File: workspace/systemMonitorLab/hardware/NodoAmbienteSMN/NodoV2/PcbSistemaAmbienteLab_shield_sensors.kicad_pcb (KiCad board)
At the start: 2 copper layers, 4 parts, among them J4 Molex_Sensor_BMP280, J5 Molex_Sensor_DHT22, U3 DHT22, U4 Bmp280Module

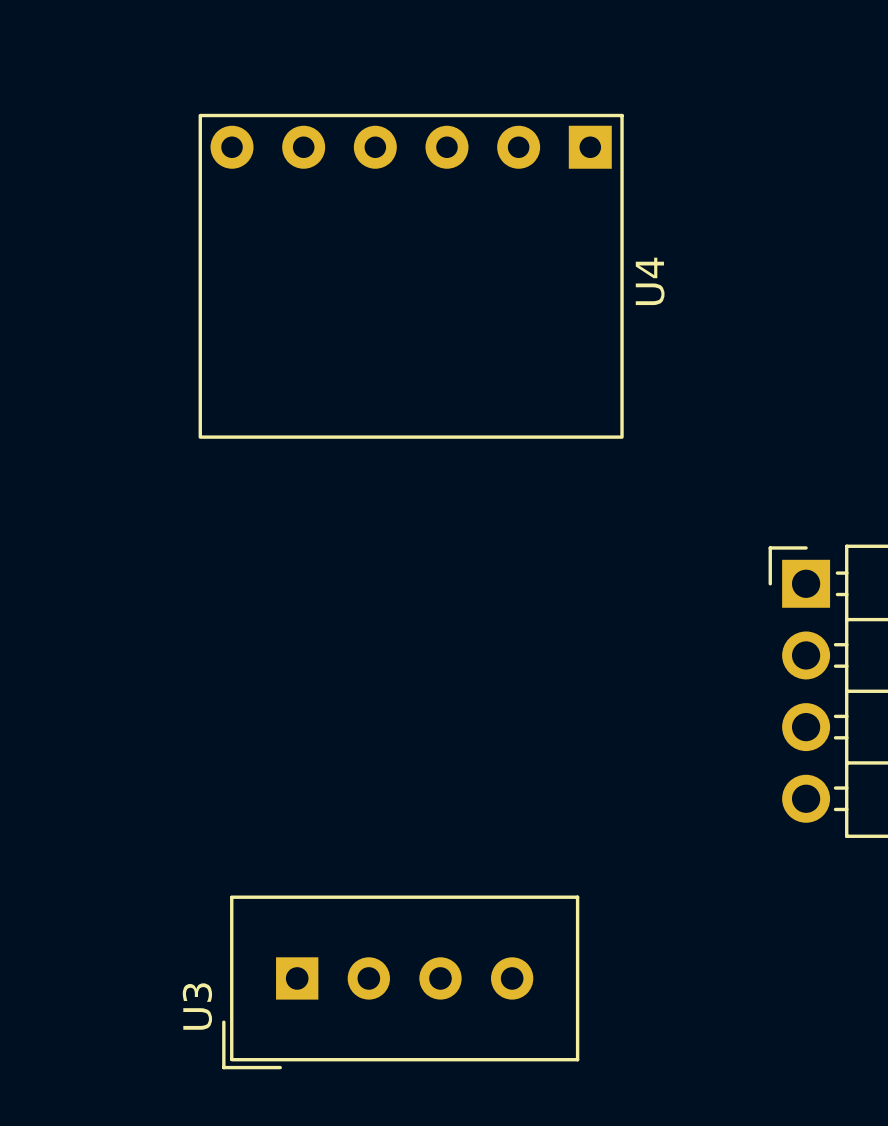
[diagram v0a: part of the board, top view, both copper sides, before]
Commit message: Se termino de generar el diseño de la placa shield_main_board.
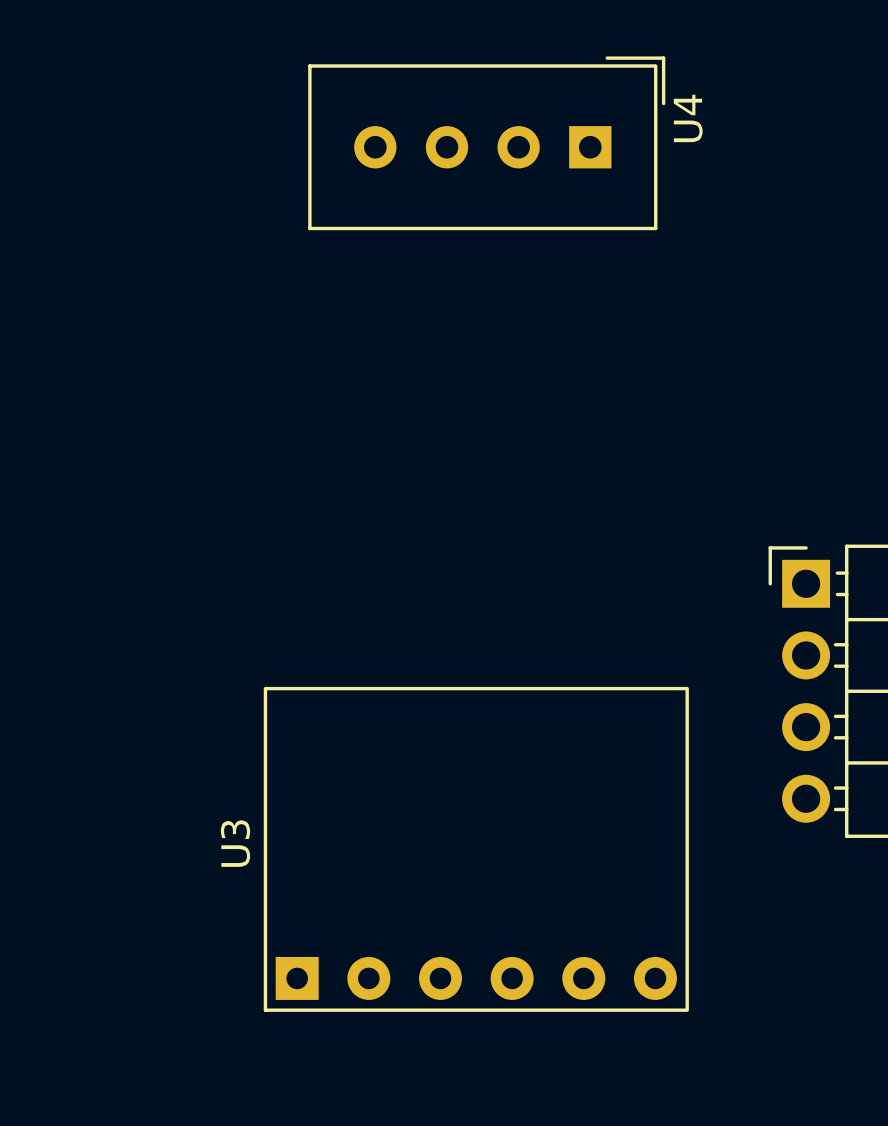
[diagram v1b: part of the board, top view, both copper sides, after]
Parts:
- U3: value DHT22 -> Bmp280Module; footprint Sensor:Aosong_DHT11_5.5x12.0_P2.54mm -> Sensors_commercial:BMP280_Module
- U4: value Bmp280Module -> DHT22; footprint Modulos:BMP280_Module -> Sensor:Aosong_DHT11_5.5x12.0_P2.54mm
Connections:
- U3 pad 2: Net-(J5-Pad2) -> GND
- U3 pad 3: unconnected-(U3-Pad3) -> Net-(J7-Pin_3)
- U3 pad 4: GND -> Net-(J7-Pin_4)
- U4 pad 1: 3V3 -> GND
- U4 pad 2: GND -> Net-(J9-Pin_2)
- U4 pad 3: Net-(J4-Pad3) -> unconnected-(U4-NC-Pad3)
- U4 pad 4: Net-(J4-Pad4) -> 3V3

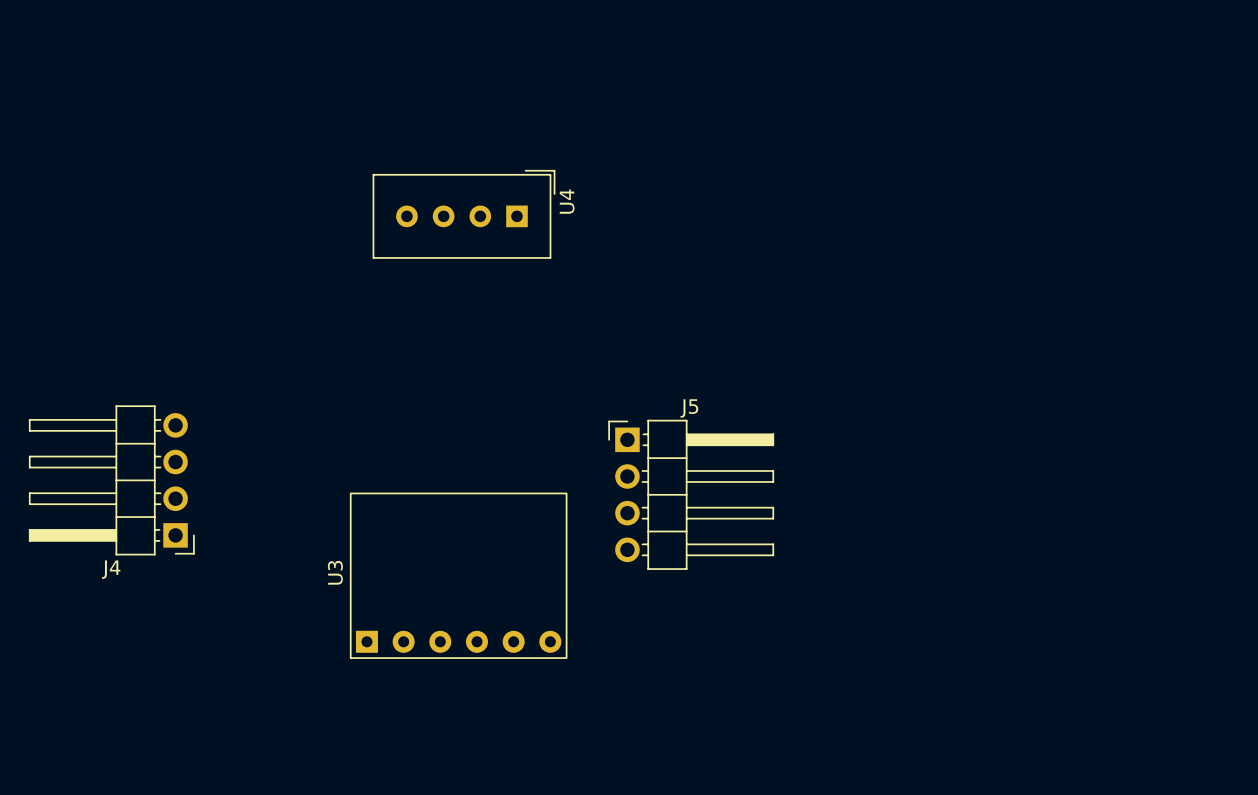
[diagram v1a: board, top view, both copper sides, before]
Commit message: Subo modificaciones en el PCB shield_sensors
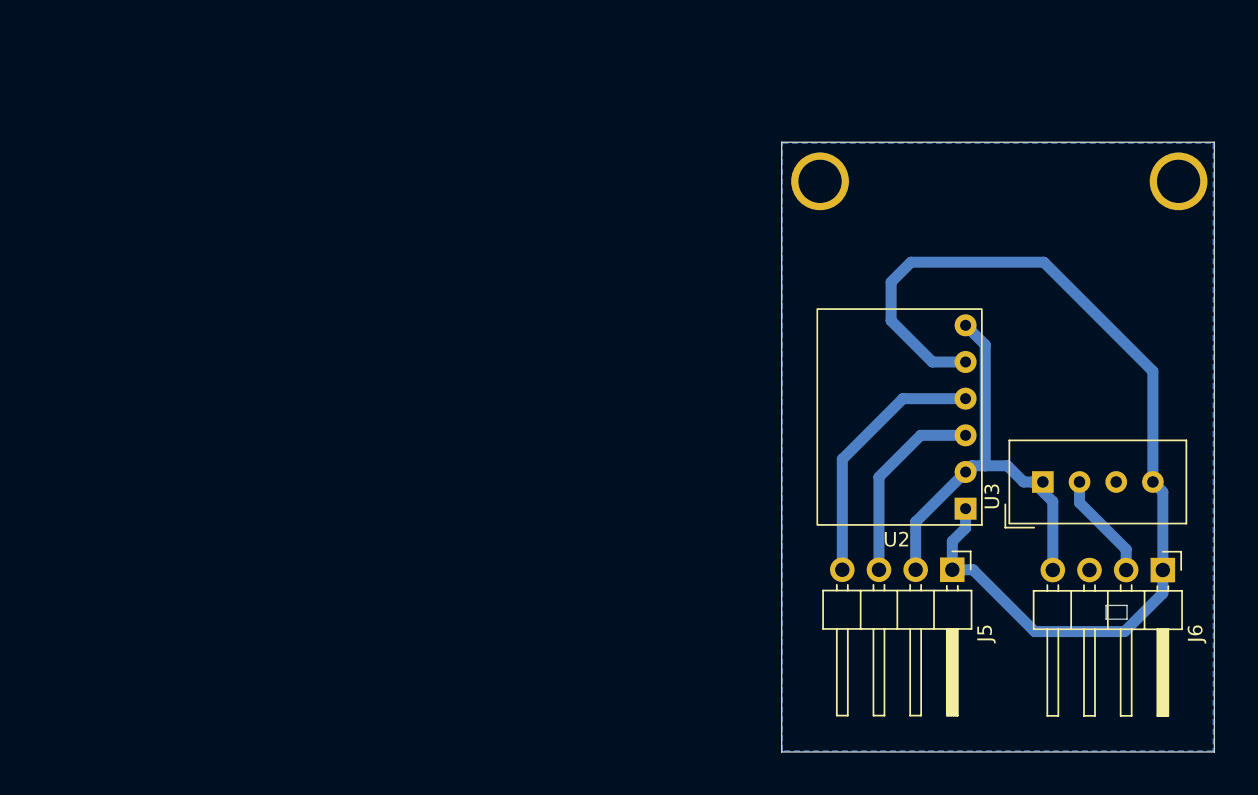
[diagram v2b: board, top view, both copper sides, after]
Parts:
- removed J4: Molex_Sensor_BMP280, Connector_PinHeader_2.54mm:PinHeader_1x04_P2.54mm_Horizontal
- removed U4: DHT22, Sensor:Aosong_DHT11_5.5x12.0_P2.54mm
- added ?: , , F.Cu at (155.7, 59.4)
- added ?: , , F.Cu at (180.6, 59.3)
- added J6: Molex_Sensor_DHT22, Connector_PinHeader_2.54mm:PinHeader_1x04_P2.54mm_Horizontal, F.Cu at (179.5, 86.3)
- added U2: Bmp280Module, Sensors_commercial:BMP280_Module, F.Cu at (165.8, 82.1)
- J5: value Molex_Sensor_DHT22 -> Molex_Sensor_BMP280
- U3: value Bmp280Module -> DHT22; footprint Sensors_commercial:BMP280_Module -> Sensor:Aosong_DHT11_5.5x12.0_P2.54mm
- moved U3 48.1 mm to (171.2, 80.2)
- moved J5 24.2 mm to (164.9, 86.3), turned to -90 degrees
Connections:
- J5 pad 2: Net-(J5-Pad2) -> GND
- J5 pad 3: unconnected-(J5-Pad3) -> Net-(J5-Pin_3)
- J5 pad 4: GND -> Net-(J5-Pin_4)
- U3 pad 1: 3V3 -> GND
- U3 pad 2: GND -> Net-(J6-Pin_2)
- U3 pad 3: Net-(J7-Pin_3) -> unconnected-(U3-NC-Pad3)
- U3 pad 4: Net-(J7-Pin_4) -> 3V3
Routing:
- net 3V3: track 0.00 -> 68.6 mm
- net GND: track 0.00 -> 31.1 mm
- net Net-(J5-Pin_4): track 0.00 -> 17.9 mm
- net Net-(J5-Pin_3): track 0.00 -> 13.6 mm
- net Net-(J6-Pin_2): track 0.00 -> 7.44 mm
- added copper zone on B.Cu, net GND
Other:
- board outline added: 30 x 42.2 mm

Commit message: Agregamos el pcb de los Leds, el siguiente paso es ver los conectores Molex comerciales y ajustar el PCB en base a esa dimensiones
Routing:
- net GND: track 31.1 -> 35.8 mm
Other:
- outline, holes or cut-outs redrawn
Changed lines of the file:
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@@
 		)
 		(fp_text user "${REFERENCE}"
-			(at 2.77 3.81 0)
+			(at 2.45 -2.02 0)
 			(layer "F.Fab")
 			(effects
@@
 		(pad "1" thru_hole rect
 			(at 0 0 270)
-			(size 1.7 1.7)
+			(size 2 2)
 			(drill 1)
 			(layers "*.Cu" "*.Mask")
@@
 		(pad "2" thru_hole oval
 			(at 0 2.54 270)
-			(size 1.7 1.7)
+			(size 2 2)
 			(drill 1)
 			(layers "*.Cu" "*.Mask")
@@
 		(pad "3" thru_hole oval
 			(at 0 5.08 270)
-			(size 1.7 1.7)
+			(size 2 2)
 			(drill 1)
 			(layers "*.Cu" "*.Mask")
@@
 		(pad "4" thru_hole oval
 			(at 0 7.62 270)
-			(size 1.7 1.7)
+			(size 2 2)
 			(drill 1)
 			(layers "*.Cu" "*.Mask")
@@
 		)
 		(fp_text user "${REFERENCE}"
-			(at 0 3.81 90)
+			(at 1.8 3.81 90)
 			(layer "F.Fab")
 			(effects
@@
 		(pad "1" thru_hole rect
 			(at 0 0 90)
-			(size 1.5 1.5)
-			(drill 0.8)
+			(size 2 2)
+			(drill 1)
 			(layers "*.Cu" "*.Mask")
 			(remove_unused_layers no)
@@
 		(pad "2" thru_hole circle
 			(at 0 2.54 90)
-			(size 1.5 1.5)
-			(drill 0.8)
+			(size 2 2)
+			(drill 1)
 			(layers "*.Cu" "*.Mask")
 			(remove_unused_layers no)
@@
 		(pad "3" thru_hole circle
 			(at 0 5.08 90)
-			(size 1.5 1.5)
-			(drill 0.8)
+			(size 2 2)
+			(drill 1)
 			(layers "*.Cu" "*.Mask")
 			(remove_unused_layers no)
@@
 		(pad "4" thru_hole circle
 			(at 0 7.62 90)
-			(size 1.5 1.5)
-			(drill 0.8)
+			(size 2 2)
+			(drill 1)
 			(layers "*.Cu" "*.Mask")
 			(remove_unused_layers no)
@@
 		(pad "1" thru_hole rect
 			(at 0 0 270)
-			(size 1.7 1.7)
+			(size 2 2)
 			(drill 1)
 			(layers "*.Cu" "*.Mask")
@@
 		(pad "2" thru_hole oval
 			(at 0 2.54 270)
-			(size 1.7 1.7)
+			(size 2 2)
 			(drill 1)
 			(layers "*.Cu" "*.Mask")
@@
 		(pad "3" thru_hole oval
 			(at 0 5.08 270)
-			(size 1.7 1.7)
+			(size 2 2)
 			(drill 1)
 			(layers "*.Cu" "*.Mask")
@@
 		(pad "4" thru_hole oval
 			(at 0 7.62 270)
-			(size 1.7 1.7)
+			(size 2 2)
 			(drill 1)
 			(layers "*.Cu" "*.Mask")
@@
 		(pad "1" thru_hole rect
 			(at 0 0 180)
-			(size 1.524 1.524)
-			(drill 0.762)
+			(size 2 2)
+			(drill 1)
 			(layers "*.Cu" "*.Mask")
 			(remove_unused_layers no)
@@
 		(pad "2" thru_hole circle
 			(at 0 2.54 180)
-			(size 1.524 1.524)
-			(drill 0.762)
+			(size 2 2)
+			(drill 1)
 			(layers "*.Cu" "*.Mask")
 			(remove_unused_layers no)
@@
 		(pad "3" thru_hole circle
 			(at 0 5.08 180)
-			(size 1.524 1.524)
-			(drill 0.762)
+			(size 2 2)
+			(drill 1)
 			(layers "*.Cu" "*.Mask")
 			(remove_unused_layers no)
@@
 		(pad "4" thru_hole circle
 			(at 0 7.62 180)
-			(size 1.524 1.524)
-			(drill 0.762)
+			(size 2 2)
+			(drill 1)
 			(layers "*.Cu" "*.Mask")
 			(remove_unused_layers no)
@@
 		(pad "5" thru_hole circle
 			(at 0 10.16 180)
-			(size 1.524 1.524)
-			(drill 0.762)
+			(size 2 2)
+			(drill 1)
 			(layers "*.Cu" "*.Mask")
 			(remove_unused_layers no)
@@
 		(pad "6" thru_hole circle
 			(at 0 12.7 180)
-			(size 1.524 1.524)
-			(drill 0.762)
+			(size 2 2)
+			(drill 1)
 			(layers "*.Cu" "*.Mask")
 			(remove_unused_layers no)
@@
 			(width 0.05)
 			(type solid)
-		)
-		(fill no)
-		(layer "Edge.Cuts")
-	)
-	(gr_rect
-		(start 175.55 88.8)
-		(end 177 89.75)
-		(stroke
-			(width 0.05)
-			(type default)
 		)
 		(fill no)
@@
 		)
 	)
+	(dimension
+		(type orthogonal)
+		(layer "Dwgs.User")
+		(pts
+			(xy 183.05 56.72) (xy 183.05 98.95)
+		)
+		(height 6.95)
+		(orientation 1)
+		(format
+			(prefix "")
+			(suffix "")
+			(units 3)
+			(units_format 1)
+			(precision 4)
+		)
+		(style
+			(thickness 0.1)
+			(arrow_length 1.27)
+			(text_position_mode 0)
+			(arrow_direction outward)
+			(extension_height 0.58642)
+			(extension_offset 0.5)
+			(keep_text_aligned yes)
+		)
+		(gr_text "42.2300 mm"
+			(at 188.85 77.835 90)
+			(layer "Dwgs.User")
+			(effects
+				(font
+					(size 1 1)
+					(thickness 0.15)
+				)
+			)
+		)
+	)
 	(segment
 		(start 160.66 66.41)
@@
 	)
 	(segment
-		(start 162.36 83.02)
-		(end 162.36 86.33)
-		(width 0.762)
-		(layer "B.Cu")
-		(net 3)
-	)
-	(segment
-		(start 167.1791 70.7591)
-		(end 167.1791 79.129)
+		(start 169.75 70.4)
+		(end 169.75 76.5581)
 		(width 0.762)
 		(layer "B.Cu")
@@
 	)
 	(segment
-		(start 165.82 69.4)
-		(end 167.1791 70.7591)
-		(width 0.762)
-		(layer "B.Cu")
-		(net 3)
-	)
-	(segment
 		(start 170.5037 80.25)
 		(end 169.8373 80.25)
@@
 	)
 	(segment
-		(start 165.82 79.56)
-		(end 162.36 83.02)
+		(start 162.36 81.59)
+		(end 162.36 86.33)
+		(width 0.762)
+		(layer "B.Cu")
+		(net 3)
+	)
+	(segment
+		(start 165.82 69.4)
+		(end 168.75 69.4)
+		(width 0.762)
+		(layer "B.Cu")
+		(net 3)
+	)
+	(segment
+		(start 168.75 69.4)
+		(end 169.75 70.4)
 		(width 0.762)
 		(layer "B.Cu")
@@
 	)
 	(segment
+		(start 169.75 76.5581)
+		(end 167.1791 79.129)
+		(width 0.762)
+		(layer "B.Cu")
+		(net 3)
+	)
+	(segment
+		(start 165.82 79.56)
+		(end 164.39 79.56)
+		(width 0.762)
+		(layer "B.Cu")
+		(net 3)
+	)
+	(segment
 		(start 171.17 80.25)
 		(end 170.5037 80.25)
+		(width 0.762)
+		(layer "B.Cu")
+		(net 3)
+	)
+	(segment
+		(start 164.39 79.56)
+		(end 162.36 81.59)
 		(width 0.762)
 		(layer "B.Cu")
@@
 		(filled_areas_thickness no)
 		(fill yes
-			(thermal_gap 0.25)
-			(thermal_bridge_width 3)
+			(thermal_gap 0.1)
+			(thermal_bridge_width 2)
 		)
 		(polygon
 			(pts
-				(xy 153.14 56.78) (xy 182.97 56.78) (xy 182.97 98.84) (xy 182.93 98.88) (xy 153.13 98.88) (xy 153.13 56.79)
-			)
-		)
+				(xy 153.15 56.75) (xy 183 56.75) (xy 183.05 98.9) (xy 153.1 98.9)
+			)
+		)

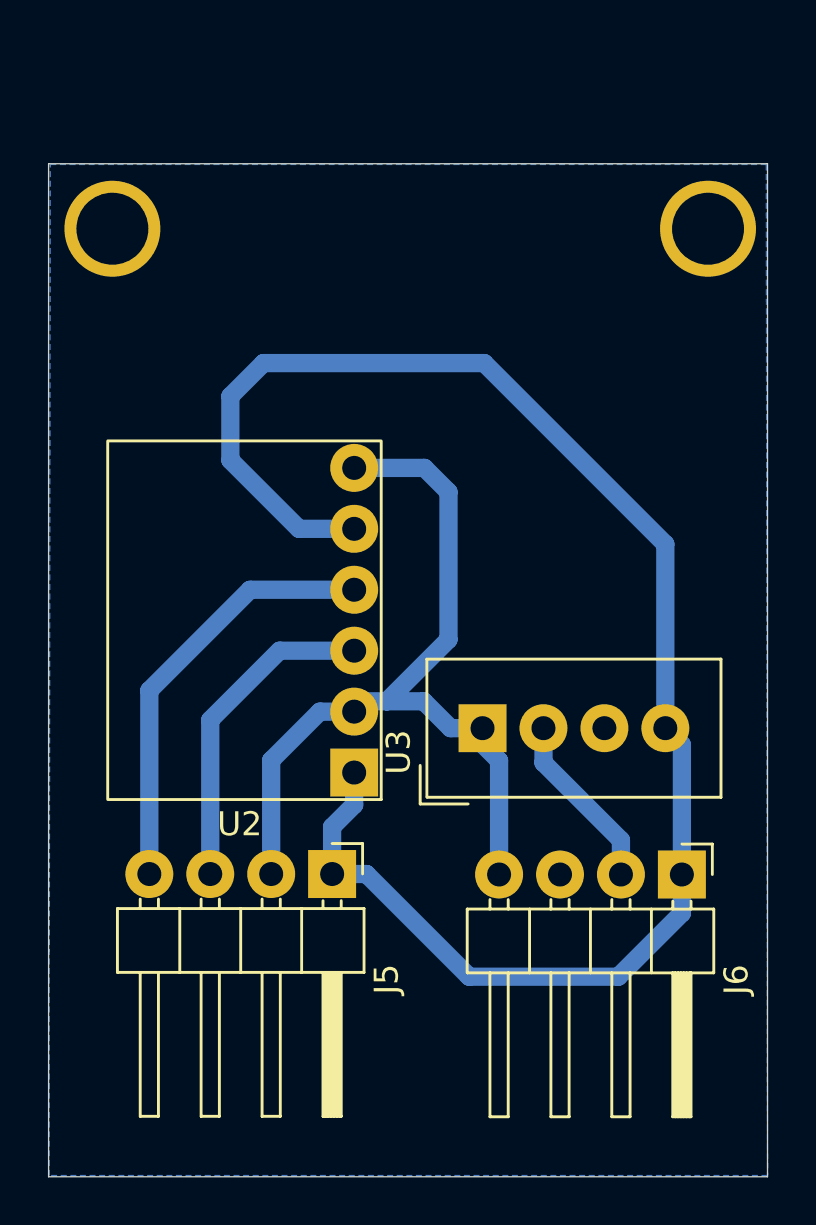
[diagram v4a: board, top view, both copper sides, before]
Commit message: Se termino de diseñar la version 2 del nodo ambiente, ahora se va a diseñar el case3d para que contenga al mismo
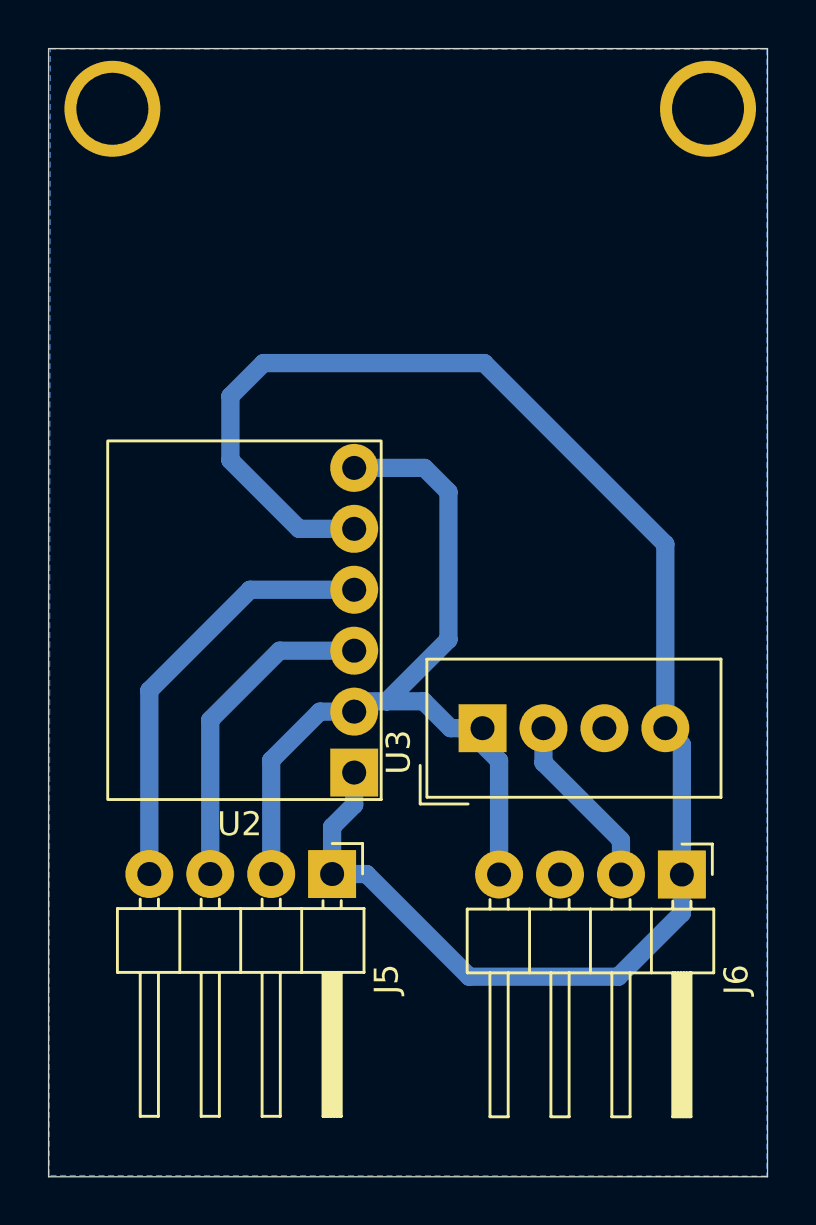
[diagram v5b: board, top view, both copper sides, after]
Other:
- board size 30 x 42.2 mm -> 30 x 47 mm
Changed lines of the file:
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@@
 		)
 		(pad "" thru_hole circle
-			(at 0 0 180)
+			(at 0 -5 180)
 			(size 4 4)
 			(drill 3)
@@
 		)
 		(pad "" thru_hole circle
-			(at 0 0.15 180)
+			(at 0 -4.85 180)
 			(size 4 4)
 			(drill 3)
@@
 	)
 	(gr_rect
-		(start 153.08 56.72)
+		(start 153.08 51.92)
 		(end 183.05 98.95)
 		(stroke
@@
 		)
 	)
-	(dimension
-		(type orthogonal)
-		(layer "Dwgs.User")
-		(pts
-			(xy 183.05 56.72) (xy 183.05 98.95)
-		)
-		(height 6.95)
-		(orientation 1)
-		(format
-			(prefix "")
-			(suffix "")
-			(units 3)
-			(units_format 1)
-			(precision 4)
-		)
-		(style
-			(thickness 0.1)
-			(arrow_length 1.27)
-			(text_position_mode 0)
-			(arrow_direction outward)
-			(extension_height 0.58642)
-			(extension_offset 0.5)
-			(keep_text_aligned yes)
-		)
-		(gr_text "42.2300 mm"
-			(at 188.85 77.835 90)
-			(layer "Dwgs.User")
-			(effects
-				(font
-					(size 1 1)
-					(thickness 0.15)
-				)
-			)
-		)
-	)
 	(segment
 		(start 160.66 66.41)
@@
 		(filled_areas_thickness no)
 		(fill yes
-			(thermal_gap 0.1)
-			(thermal_bridge_width 2)
+			(thermal_gap 0.5)
+			(thermal_bridge_width 0.5)
 		)
 		(polygon
 			(pts
-				(xy 153.15 56.75) (xy 183 56.75) (xy 183.05 98.9) (xy 153.1 98.9)
-			)
-		)
+				(xy 153.15 51.925) (xy 183.025 51.95) (xy 183.025 98.925) (xy 153.1 98.9)
+			)
+		)
